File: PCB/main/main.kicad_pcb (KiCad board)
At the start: 2 copper layers, 121.9 x 91.4 mm, 47 parts, among them IC1 LM358DT, IC2 LM358DT, IC3 AT24C256C-SSHL-T, J1 Conn_01x33_Female, J2 Conn_01x33_Female, J3 Conn_01x33_Female, J4 Conn_01x33_Female, J5 47346-0001, J5 USB_B_Micro, Q1 IRF9540NPbF, U1 MCP73831-2-OT, U2 FT232RL, U3 MCP1700-3302E_TO92

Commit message: main modified by masonwabe
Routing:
- net +3v3: track 143.9 -> 127.6 mm, vias 12 -> 13
- added copper zone on B.Cu, net +3v3
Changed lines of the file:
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@@
   (segment (start 142.283964 87.34844) (end 142.283964 88.106036) (width 0.25) (layer "F.Cu") (net 64))
   (segment (start 158.42298 96.74452) (end 158.3975 96.77) (width 0.25) (layer "F.Cu") (net 64))
-  (segment (start 145.75 104.139989) (end 147.783011 104.139989) (width 0.25) (layer "F.Cu") (net 64))
   (segment (start 157.4 93.24) (end 157.4 92.725) (width 0.25) (layer "F.Cu") (net 64))
   (segment (start 147.955 102.095402) (end 147.975201 102.075201) (width 0.25) (layer "F.Cu") (net 64))
@@
   (segment (start 146.6 84.775) (end 146.828 84.775) (width 0.25) (layer "F.Cu") (net 64))
   (segment (start 159.200006 96.77) (end 159.45952 96.510486) (width 0.25) (layer "F.Cu") (net 64))
-  (segment (start 140.25 109.22) (end 144.0555 105.4145) (width 0.25) (layer "F.Cu") (net 64))
   (segment (start 159.200006 97.77) (end 158.3975 97.77) (width 0.25) (layer "F.Cu") (net 64))
-  (segment (start 144.0555 105.4145) (end 144.0555 104.14) (width 0.25) (layer "F.Cu") (net 64))
   (segment (start 159.200006 93.77) (end 158.3975 93.77) (width 0.25) (layer "F.Cu") (net 64))
   (segment (start 165.31 99.879994) (end 165.050486 99.62048) (width 0.25) (layer "F.Cu") (net 64))
@@
   (via (at 157.4 92.725) (size 0.8) (drill 0.4) (layers "F.Cu" "B.Cu") (net 64))
   (via (at 147.714918 86.263081) (size 0.8) (drill 0.4) (layers "F.Cu" "B.Cu") (net 64))
-  (via (at 145.75 104.139989) (size 0.8) (drill 0.4) (layers "F.Cu" "B.Cu") (net 64))
-  (via (at 144.0555 104.14) (size 0.8) (drill 0.4) (layers "F.Cu" "B.Cu") (net 64))
+  (via (at 137.16 109.22) (size 0.8) (drill 0.4) (layers "F.Cu" "B.Cu") (net 64))
   (via (at 152.394219 94.758317) (size 0.8) (drill 0.4) (layers "F.Cu" "B.Cu") (net 64))
   (via (at 146.6 84.775) (size 0.8) (drill 0.4) (layers "F.Cu" "B.Cu") (net 64))
@@
   (via (at 121.92 93.98) (size 0.8) (drill 0.4) (layers "F.Cu" "B.Cu") (net 64))
   (via (at 121.92 83.82) (size 0.8) (drill 0.4) (layers "F.Cu" "B.Cu") (net 64))
+  (via (at 147.955 104.139978) (size 0.8) (drill 0.4) (layers "F.Cu" "B.Cu") (net 64))
   (via (at 142.283964 87.34844) (size 0.8) (drill 0.4) (layers "F.Cu" "B.Cu") (net 64))
-  (segment (start 150.752595 101.150469) (end 152.394219 99.508845) (width 0.25) (layer "B.Cu") (net 64))
+  (via (at 149.852758 93.972758) (size 0.8) (drill 0.4) (layers "F.Cu" "B.Cu") (net 64))
   (segment (start 154.325 84.775) (end 146.6 84.775) (width 0.25) (layer "B.Cu") (net 64))
   (segment (start 125.184511 80.555489) (end 121.92 83.82) (width 0.25) (layer "B.Cu") (net 64))
   (segment (start 159.444511 90.680489) (end 159.444511 80.979897) (width 0.25) (layer "B.Cu") (net 64))
-  (segment (start 150.3637 101.150469) (end 150.752595 101.150469) (width 0.25) (layer "B.Cu") (net 64))
   (segment (start 122.919503 84.819503) (end 122.919503 92.980497) (width 0.25) (layer "B.Cu") (net 64))
   (segment (start 142.782893 86.849511) (end 142.283964 87.34844) (width 0.25) (layer "B.Cu") (net 64))
-  (segment (start 147.975201 102.075201) (end 149.675969 102.075201) (width 0.25) (layer "B.Cu") (net 64))
   (segment (start 122.919503 92.980497) (end 121.92 93.98) (width 0.25) (layer "B.Cu") (net 64))
   (segment (start 159.444511 80.979897) (end 159.020103 80.555489) (width 0.25) (layer "B.Cu") (net 64))
-  (segment (start 145.749989 104.14) (end 145.75 104.139989) (width 0.25) (layer "B.Cu") (net 64))
   (segment (start 159.020103 80.555489) (end 158.099239 80.555489) (width 0.25) (layer "B.Cu") (net 64))
-  (segment (start 144.0555 104.14) (end 145.749989 104.14) (width 0.25) (layer "B.Cu") (net 64))
-  (segment (start 152.394219 99.508845) (end 152.394219 94.758317) (width 0.25) (layer "B.Cu") (net 64))
   (segment (start 142.964511 82.004511) (end 141.515489 80.555489) (width 0.25) (layer "B.Cu") (net 64))
   (segment (start 137.884511 84.544511) (end 142.540103 84.544511) (width 0.25) (layer "B.Cu") (net 64))
   (segment (start 158.099239 80.555489) (end 155.664511 82.990217) (width 0.25) (layer "B.Cu") (net 64))
-  (segment (start 149.675969 101.838199) (end 150.3637 101.150469) (width 0.25) (layer "B.Cu") (net 64))
+  (segment (start 149.86 93.98) (end 149.852758 93.972758) (width 0.25) (layer "B.Cu") (net 64))
   (segment (start 142.964511 84.120103) (end 142.964511 82.004511) (width 0.25) (layer "B.Cu") (net 64))
   (segment (start 157.4 92.725) (end 159.444511 90.680489) (width 0.25) (layer "B.Cu") (net 64))
@@
   (segment (start 147.714918 86.263081) (end 147.128488 86.849511) (width 0.25) (layer "B.Cu") (net 64))
   (segment (start 142.540103 84.544511) (end 142.964511 84.120103) (width 0.25) (layer "B.Cu") (net 64))
-  (segment (start 149.675969 102.075201) (end 149.675969 101.838199) (width 0.25) (layer "B.Cu") (net 64))
   (segment (start 121.92 83.82) (end 122.919503 84.819503) (width 0.25) (layer "B.Cu") (net 64))
+  (segment (start 146.852484 105.242494) (end 147.955 104.139978) (width 0.25) (layer "B.Cu") (net 64))
   (segment (start 141.515489 80.555489) (end 125.184511 80.555489) (width 0.25) (layer "B.Cu") (net 64))
+  (segment (start 152.394219 94.758317) (end 151.615902 93.98) (width 0.25) (layer "B.Cu") (net 64))
+  (segment (start 151.615902 93.98) (end 149.86 93.98) (width 0.25) (layer "B.Cu") (net 64))
   (segment (start 126.79569 99.26431) (end 129.33569 99.26431) (width 0.25) (layer "F.Cu") (net 65))
   (segment (start 125.21 83.82) (end 126.940498 83.82) (width 0.25) (layer "F.Cu") (net 65))
@@
     (connect_pads (clearance 0.508))
     (min_thickness 0.254) (filled_areas_thickness no)
+    (fill yes (thermal_gap 0.508) (thermal_bridge_width 0.508))
+    (polygon
+      (pts
+        (xy 101.6 58.42)
+        (xy 190.5 58.42)
+        (xy 190.5 134.62)
+        (xy 101.6 134.62)
+        (xy 101.6 147.32)
+        (xy 63.5 147.32)
+        (xy 63.5 50.8)
+        (xy 101.6 50.8)
+      )
+    )
+  )
+  (zone (net 64) (net_name "+3v3") (layer "B.Cu") (hatch edge 0.508)
+    (connect_pads (clearance 0.508))
+    (min_thickness 0.254) (filled_areas_thickness no)

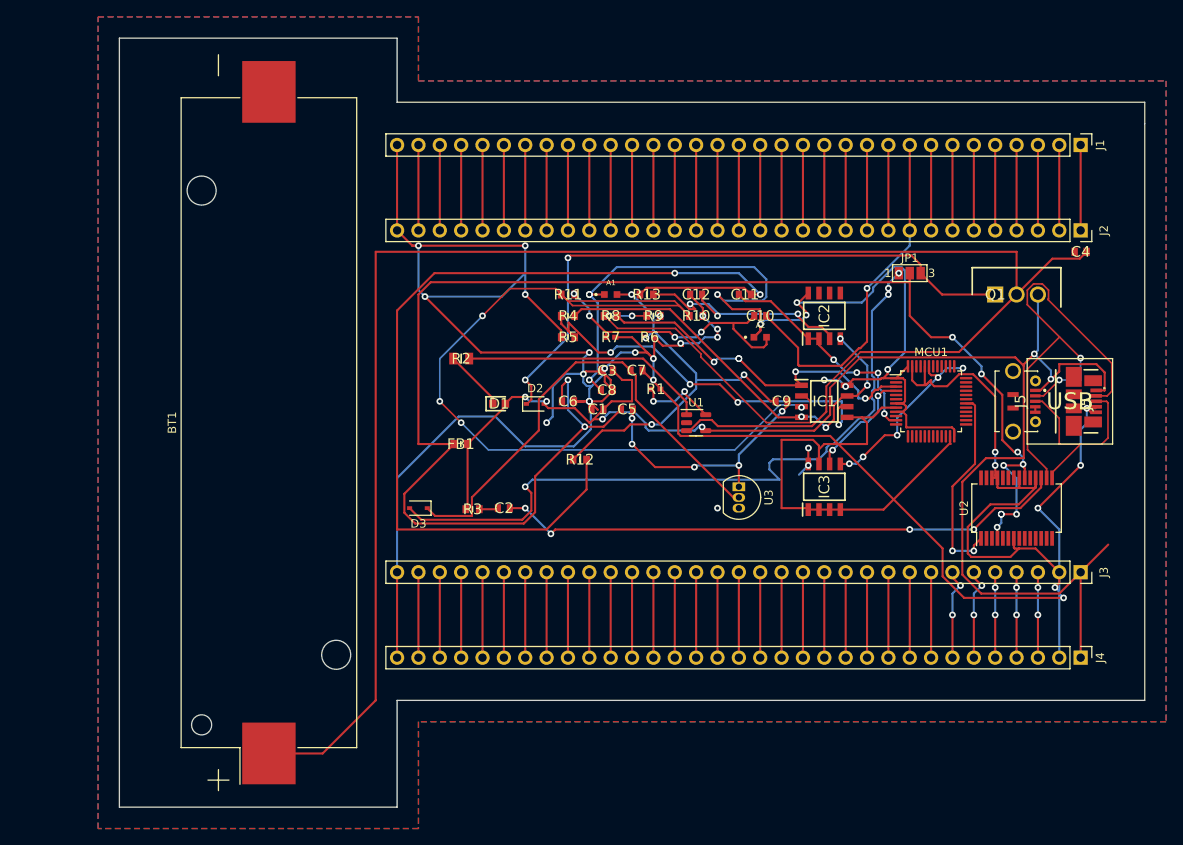
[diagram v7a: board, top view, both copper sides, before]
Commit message: updated PCB with mount holes
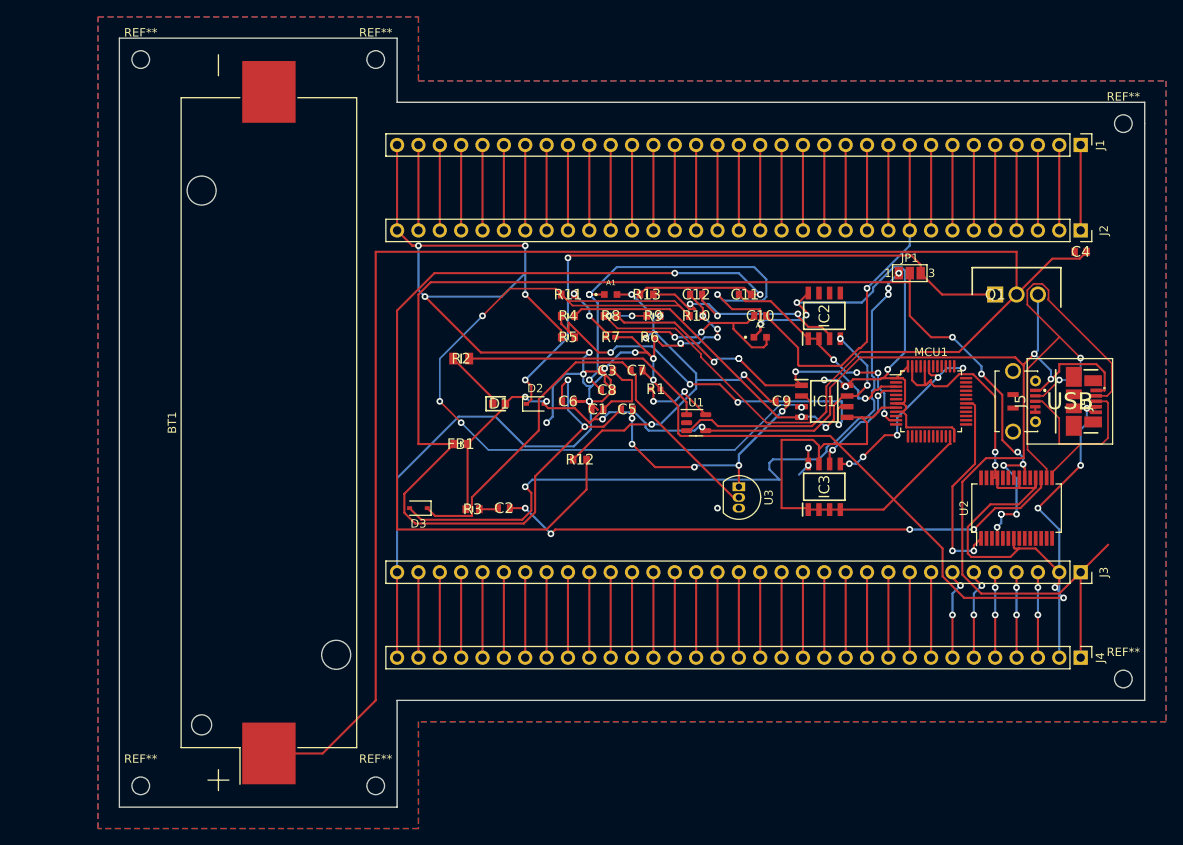
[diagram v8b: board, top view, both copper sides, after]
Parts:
- added REF**: MountingHole_2.1mm, MountingHole:MountingHole_2.1mm, F.Cu at (96.5, 142.2)
- added REF**: MountingHole_2.1mm, MountingHole:MountingHole_2.1mm, F.Cu at (185.4, 63.5)
- added REF**: MountingHole_2.1mm, MountingHole:MountingHole_2.1mm, F.Cu at (68.6, 55.9)
- added REF**: MountingHole_2.1mm, MountingHole:MountingHole_2.1mm, F.Cu at (68.6, 142.2)
- added REF**: MountingHole_2.1mm, MountingHole:MountingHole_2.1mm, F.Cu at (185.4, 129.5)
- added REF**: MountingHole_2.1mm, MountingHole:MountingHole_2.1mm, F.Cu at (96.5, 55.9)
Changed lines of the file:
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@@
     )
+  )
+  (footprint "MountingHole:MountingHole_2.1mm" (layer "F.Cu")
+    (at 96.52 142.24)
+    (descr "Mounting Hole 2.1mm, no annular")
+    (tags "mounting hole 2.1mm no annular")
+    (attr exclude_from_pos_files exclude_from_bom)
+    (fp_text reference "REF**" (at 0 -3.2) (layer "F.SilkS")
+      (effects (font (size 1 1) (thickness 0.15)))
+    )
+    (fp_text value "MountingHole_2.1mm" (at 0 3.2) (layer "F.Fab")
+      (effects (font (size 1 1) (thickness 0.15)))
+    )
+    (fp_text user "${REFERENCE}" (at 0.3 0) (layer "F.Fab")
+      (effects (font (size 1 1) (thickness 0.15)))
+    )
+    (fp_circle (center 0 0) (end 2.1 0) (layer "Cmts.User") (width 0.15) (fill none))
+    (fp_circle (center 0 0) (end 2.35 0) (layer "F.CrtYd") (width 0.05) (fill none))
+    (pad "" np_thru_hole circle (at 0 0) (size 2.1 2.1) (drill 2.1) (layers *.Cu *.Mask))
   )
   (footprint "SamacSys_Parts:LEDC1608X70N" (layer "F.Cu")
@@
       (rotate (xyz 0 0 0))
     )
+  )
+  (footprint "MountingHole:MountingHole_2.1mm" (layer "F.Cu")
+    (at 185.42 63.5)
+    (descr "Mounting Hole 2.1mm, no annular")
+    (tags "mounting hole 2.1mm no annular")
+    (attr exclude_from_pos_files exclude_from_bom)
+    (fp_text reference "REF**" (at 0 -3.2) (layer "F.SilkS")
+      (effects (font (size 1 1) (thickness 0.15)))
+    )
+    (fp_text value "MountingHole_2.1mm" (at 0 3.2) (layer "F.Fab")
+      (effects (font (size 1 1) (thickness 0.15)))
+    )
+    (fp_text user "${REFERENCE}" (at 0.3 0) (layer "F.Fab")
+      (effects (font (size 1 1) (thickness 0.15)))
+    )
+    (fp_circle (center 0 0) (end 2.1 0) (layer "Cmts.User") (width 0.15) (fill none))
+    (fp_circle (center 0 0) (end 2.35 0) (layer "F.CrtYd") (width 0.05) (fill none))
+    (pad "" np_thru_hole circle (at 0 0) (size 2.1 2.1) (drill 2.1) (layers *.Cu *.Mask))
   )
   (footprint "SamacSys_Parts:RESC1608X55N" (layer "F.Cu")
@@
       (rotate (xyz -90 0 -180))
     )
+  )
+  (footprint "MountingHole:MountingHole_2.1mm" (layer "F.Cu")
+    (at 68.58 55.88)
+    (descr "Mounting Hole 2.1mm, no annular")
+    (tags "mounting hole 2.1mm no annular")
+    (attr exclude_from_pos_files exclude_from_bom)
+    (fp_text reference "REF**" (at 0 -3.2) (layer "F.SilkS")
+      (effects (font (size 1 1) (thickness 0.15)))
+    )
+    (fp_text value "MountingHole_2.1mm" (at 0 3.2) (layer "F.Fab")
+      (effects (font (size 1 1) (thickness 0.15)))
+    )
+    (fp_text user "${REFERENCE}" (at 0.3 0) (layer "F.Fab")
+      (effects (font (size 1 1) (thickness 0.15)))
+    )
+    (fp_circle (center 0 0) (end 2.1 0) (layer "Cmts.User") (width 0.15) (fill none))
+    (fp_circle (center 0 0) (end 2.35 0) (layer "F.CrtYd") (width 0.05) (fill none))
+    (pad "" np_thru_hole circle (at 0 0) (size 2.1 2.1) (drill 2.1) (layers *.Cu *.Mask))
   )
   (footprint "SamacSys_Parts_Power:TO254P469X1042X1967-3P" (layer "F.Cu")
@@
       (rotate (xyz 0 0 0))
     )
+  )
+  (footprint "MountingHole:MountingHole_2.1mm" (layer "F.Cu")
+    (at 68.58 142.24)
+    (descr "Mounting Hole 2.1mm, no annular")
+    (tags "mounting hole 2.1mm no annular")
+    (attr exclude_from_pos_files exclude_from_bom)
+    (fp_text reference "REF**" (at 0 -3.2) (layer "F.SilkS")
+      (effects (font (size 1 1) (thickness 0.15)))
+    )
+    (fp_text value "MountingHole_2.1mm" (at 0 3.2) (layer "F.Fab")
+      (effects (font (size 1 1) (thickness 0.15)))
+    )
+    (fp_text user "${REFERENCE}" (at 0.3 0) (layer "F.Fab")
+      (effects (font (size 1 1) (thickness 0.15)))
+    )
+    (fp_circle (center 0 0) (end 2.1 0) (layer "Cmts.User") (width 0.15) (fill none))
+    (fp_circle (center 0 0) (end 2.35 0) (layer "F.CrtYd") (width 0.05) (fill none))
+    (pad "" np_thru_hole circle (at 0 0) (size 2.1 2.1) (drill 2.1) (layers *.Cu *.Mask))
   )
   (footprint "SamacSys_Parts:XDCR_ALS-PT19-315C_L177_TR8" (layer "F.Cu")
@@
     )
   )
+  (footprint "MountingHole:MountingHole_2.1mm" (layer "F.Cu")
+    (at 185.42 129.54)
+    (descr "Mounting Hole 2.1mm, no annular")
+    (tags "mounting hole 2.1mm no annular")
+    (attr exclude_from_pos_files exclude_from_bom)
+    (fp_text reference "REF**" (at 0 -3.2) (layer "F.SilkS")
+      (effects (font (size 1 1) (thickness 0.15)))
+    )
+    (fp_text value "MountingHole_2.1mm" (at 0 3.2) (layer "F.Fab")
+      (effects (font (size 1 1) (thickness 0.15)))
+    )
+    (fp_text user "${REFERENCE}" (at 0.3 0) (layer "F.Fab")
+      (effects (font (size 1 1) (thickness 0.15)))
+    )
+    (fp_circle (center 0 0) (end 2.1 0) (layer "Cmts.User") (width 0.15) (fill none))
+    (fp_circle (center 0 0) (end 2.35 0) (layer "F.CrtYd") (width 0.05) (fill none))
+    (pad "" np_thru_hole circle (at 0 0) (size 2.1 2.1) (drill 2.1) (layers *.Cu *.Mask))
+  )
   (footprint "Connector_PinHeader_2.54mm:PinHeader_1x33_P2.54mm_Vertical" (layer "F.Cu")
     (at 180.34 127 -90)
@@
     )
   )
+  (footprint "MountingHole:MountingHole_2.1mm" (layer "F.Cu")
+    (at 96.52 55.88)
+    (descr "Mounting Hole 2.1mm, no annular")
+    (tags "mounting hole 2.1mm no annular")
+    (attr exclude_from_pos_files exclude_from_bom)
+    (fp_text reference "REF**" (at 0 -3.2) (layer "F.SilkS")
+      (effects (font (size 1 1) (thickness 0.15)))
+    )
+    (fp_text value "MountingHole_2.1mm" (at 0 3.2) (layer "F.Fab")
+      (effects (font (size 1 1) (thickness 0.15)))
+    )
+    (fp_text user "${REFERENCE}" (at 0.3 0) (layer "F.Fab")
+      (effects (font (size 1 1) (thickness 0.15)))
+    )
+    (fp_circle (center 0 0) (end 2.1 0) (layer "Cmts.User") (width 0.15) (fill none))
+    (fp_circle (center 0 0) (end 2.35 0) (layer "F.CrtYd") (width 0.05) (fill none))
+    (pad "" np_thru_hole circle (at 0 0) (size 2.1 2.1) (drill 2.1) (layers *.Cu *.Mask))
+  )
   (footprint "Connector_PinSocket_2.54mm:PinSocket_1x33_P2.54mm_Vertical" (layer "F.Cu")
